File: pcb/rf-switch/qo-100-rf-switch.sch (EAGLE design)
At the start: 40 parts, among them CON1 4P-SH-SIDE, U1 F2915NBGK, U2 ADP7142AUJZ-3.3, U3 MCP23008

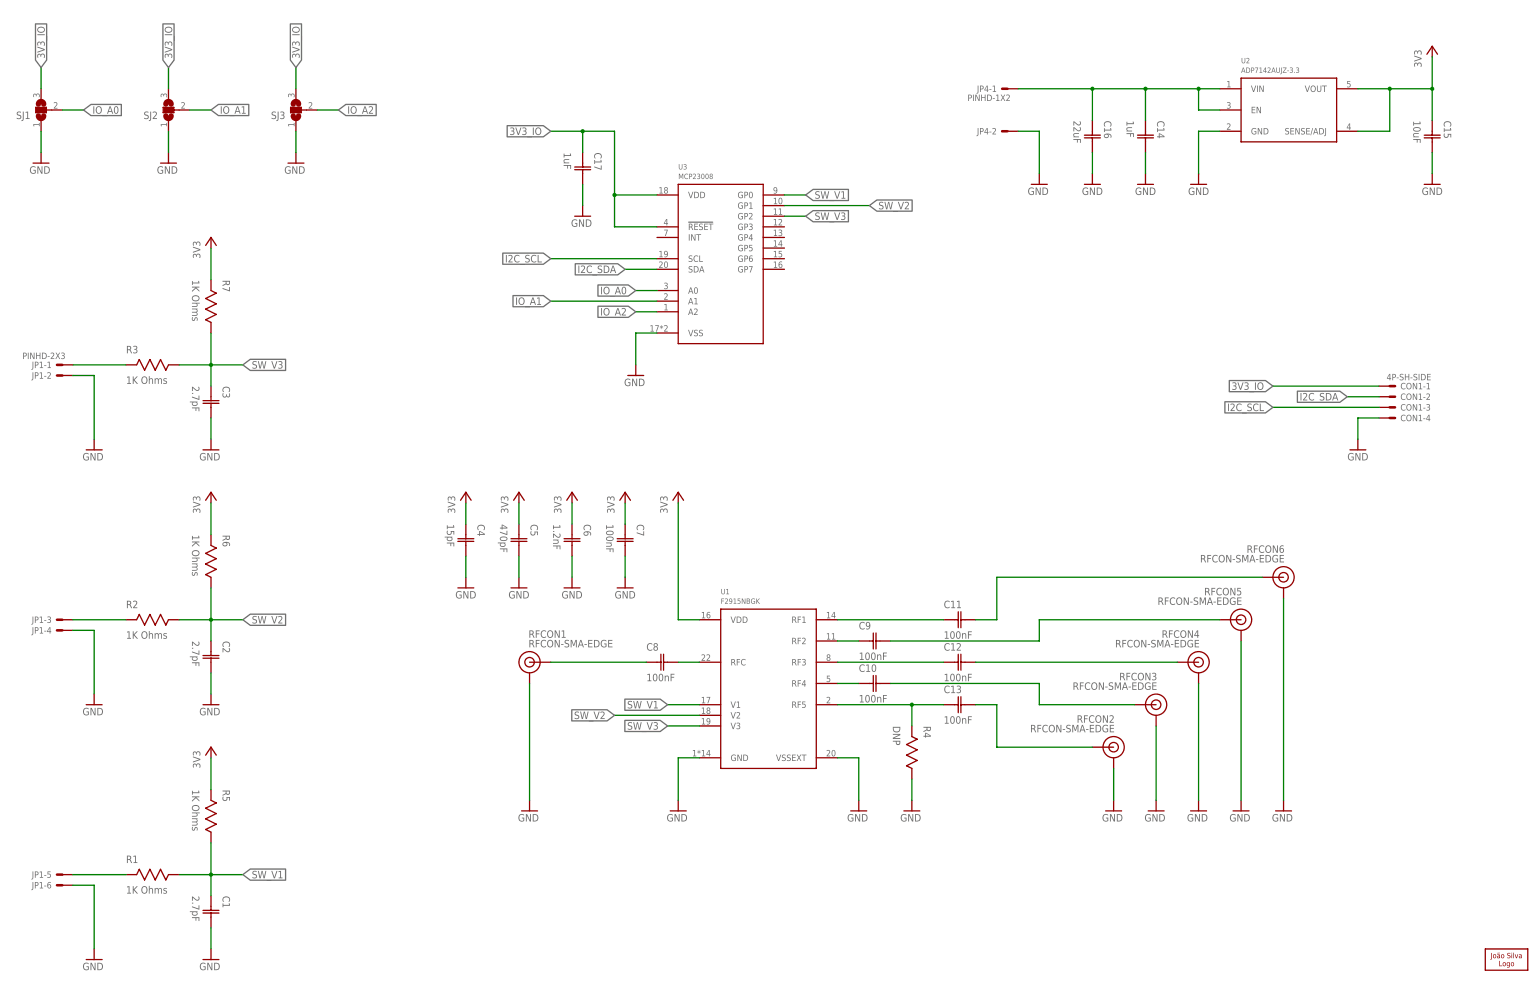
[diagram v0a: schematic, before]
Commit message: RF Switch v2: Allow chosing interface or standalone power in software
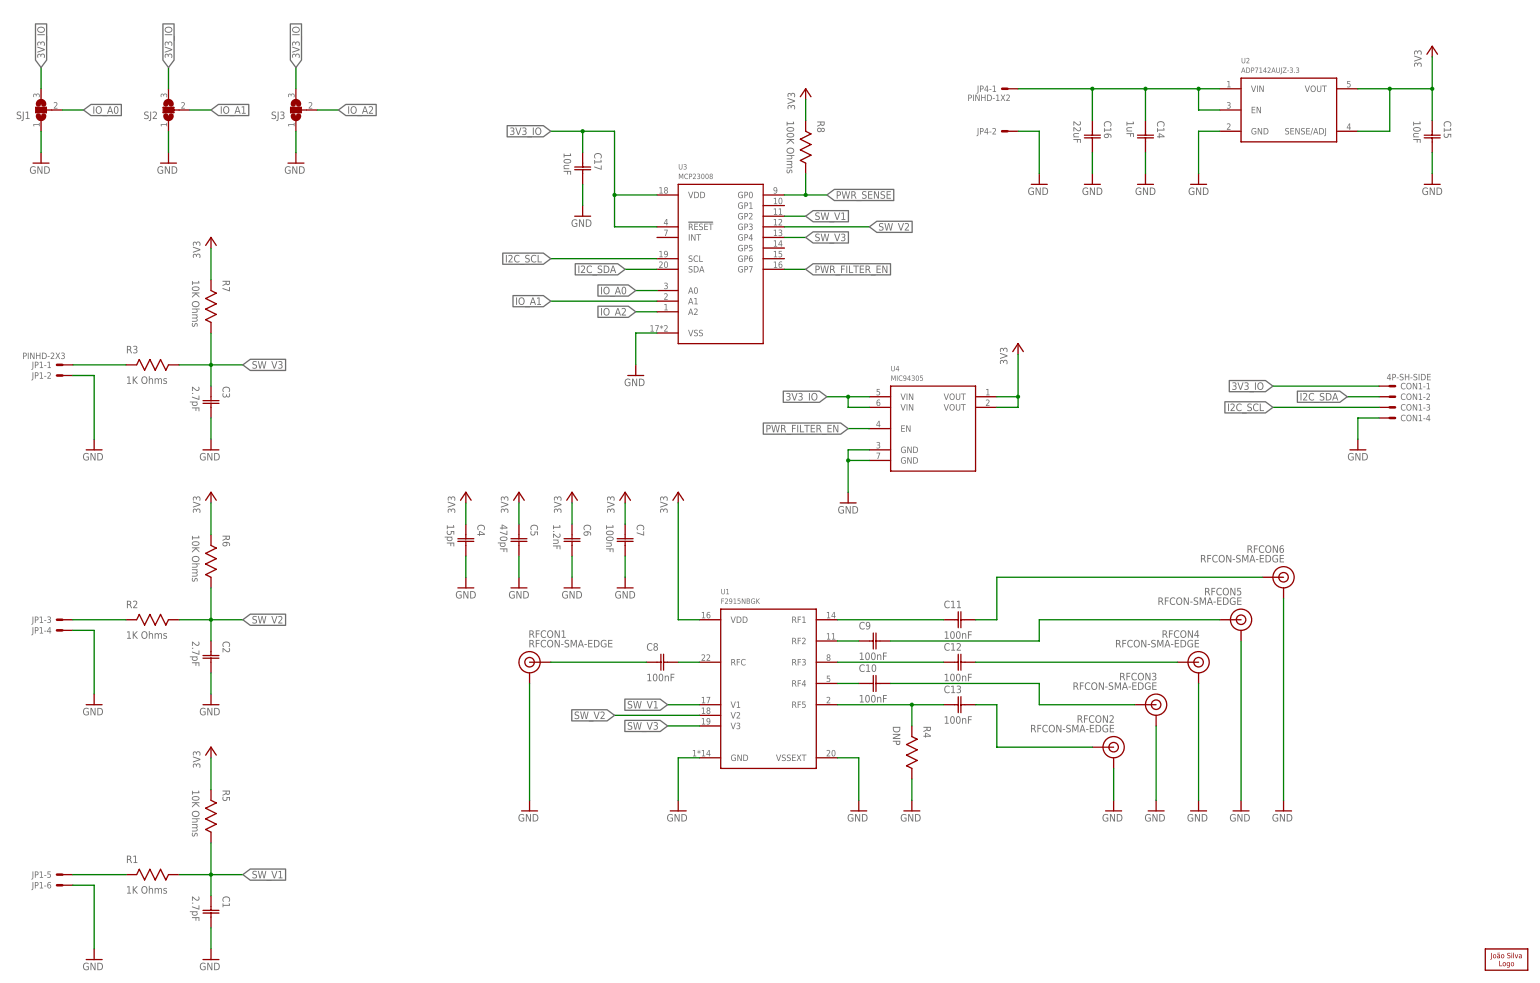
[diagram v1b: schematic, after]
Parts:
- added R8: 100K Ohms, Resistor:RESISTOR-0603
- added U4: MIC94305, Microchip:MIC94305
- C17: value 1uF -> 10uF
- R5, R6, R7: value 1K Ohms -> 10K Ohms
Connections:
- new net PWR_FILTER_EN: U3.GP7, U4.EN
- new net PWR_SENSE: R8.1, U3.GP0
- net 3V3: now also R8.2, U4.VOUT@0, U4.VOUT@1
- net 3V3_IO: now also U4.VIN@0, U4.VIN@1
- net GND: now also U4.GND@0, U4.GND@1
- net SW_V1: now also U3.GP2; no longer U3.GP0
- net SW_V2: now also U3.GP3; no longer U3.GP1
- net SW_V3: now also U3.GP4; no longer U3.GP2
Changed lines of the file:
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@@
 <attributes>
 <attribute name="CNAME" value="None"/>
-<attribute name="CREVISION" value="1"/>
+<attribute name="CREVISION" value="2"/>
 <attribute name="DESIGNER" value="Joao Silva"/>
 </attributes>
@@
 <part name="CON1" library="JST" deviceset="4P" device="-SH-SIDE"/>
 <part name="JP1" library="Pin Header" deviceset="PINHD-2X3" device="" package3d_urn="urn:adsk.eagle:package:22462/2"/>
-<part name="R5" library="Resistor" deviceset="RESISTOR" device="-0603" value="1K Ohms"/>
+<part name="R5" library="Resistor" deviceset="RESISTOR" device="-0603" value="10K Ohms"/>
 <part name="3V2" library="Supply Symbol" deviceset="3V3" device=""/>
-<part name="R6" library="Resistor" deviceset="RESISTOR" device="-0603" value="1K Ohms"/>
+<part name="R6" library="Resistor" deviceset="RESISTOR" device="-0603" value="10K Ohms"/>
 <part name="3V3" library="Supply Symbol" deviceset="3V3" device=""/>
-<part name="R7" library="Resistor" deviceset="RESISTOR" device="-0603" value="1K Ohms"/>
+<part name="R7" library="Resistor" deviceset="RESISTOR" device="-0603" value="10K Ohms"/>
 <part name="GND25" library="Supply Symbol" deviceset="GND" device=""/>
-<part name="C17" library="Capacitor" deviceset="CAPACITOR" device="-0603" value="1uF"/>
+<part name="C17" library="Capacitor" deviceset="CAPACITOR" device="-0603" value="10uF"/>
 <part name="GND26" library="Supply Symbol" deviceset="GND" device=""/>
 <part name="GND27" library="Supply Symbol" deviceset="GND" device=""/>
@@
 <part name="SJ3" library="Solder Jumper" deviceset="SJ2" device="S"/>
 <part name="GND30" library="Supply Symbol" deviceset="GND" device=""/>
+<part name="U4" library="Microchip" deviceset="MIC94305" device=""/>
+<part name="3V7" library="Supply Symbol" deviceset="3V3" device=""/>
+<part name="GND31" library="Supply Symbol" deviceset="GND" device=""/>
+<part name="R8" library="Resistor" deviceset="RESISTOR" device="-0603" value="100K Ohms"/>
+<part name="3V10" library="Supply Symbol" deviceset="3V3" device=""/>
 </parts>
 <sheets>
@@
 <attribute name="VALUE" x="81.026" y="210.82" size="1.778" layer="96"/>
 </instance>
+<instance part="U4" gate="G$1" x="246.38" y="160.02" smashed="yes">
+<attribute name="NAME" x="226.06" y="163.576" size="1.27" layer="95"/>
+<attribute name="VALUE" x="226.06" y="161.29" size="1.27" layer="96"/>
+</instance>
+<instance part="3V7" gate="G$1" x="256.54" y="167.64" smashed="yes">
+<attribute name="VALUE" x="254" y="165.1" size="1.778" layer="96" rot="R90"/>
+</instance>
+<instance part="GND31" gate="G$1" x="215.9" y="134.62" smashed="yes">
+<attribute name="VALUE" x="215.9" y="129.54" size="1.778" layer="96" align="bottom-center"/>
+</instance>
+<instance part="R8" gate="G$1" x="205.74" y="223.52" smashed="yes" rot="R270">
+<attribute name="VALUE" x="202.9714" y="223.52" size="1.778" layer="96" ratio="10" rot="SR270" align="top-left"/>
+<attribute name="NAME" x="208.5086" y="223.52" size="1.778" layer="95" ratio="10" rot="SR270"/>
+<attribute name="TOLERANCE" x="200.4314" y="223.52" size="1.778" layer="97" ratio="10" rot="SR270" align="top-left"/>
+</instance>
+<instance part="3V10" gate="G$1" x="205.74" y="228.6" smashed="yes">
+<attribute name="VALUE" x="203.2" y="226.06" size="1.778" layer="96" rot="R90"/>
+</instance>
 </instances>
 <busses>
@@
 <wire x1="83.82" y1="215.9" x2="83.82" y2="220.98" width="0.1524" layer="91"/>
 <pinref part="SJ3" gate="G$1" pin="1"/>
+</segment>
+<segment>
+<pinref part="GND31" gate="G$1" pin="GND"/>
+<wire x1="215.9" y1="134.62" x2="215.9" y2="142.24" width="0.1524" layer="91"/>
+<wire x1="215.9" y1="142.24" x2="215.9" y2="144.78" width="0.1524" layer="91"/>
+<wire x1="215.9" y1="144.78" x2="220.98" y2="144.78" width="0.1524" layer="91"/>
+<wire x1="220.98" y1="142.24" x2="215.9" y2="142.24" width="0.1524" layer="91"/>
+<junction x="215.9" y="142.24"/>
+<pinref part="U4" gate="G$1" pin="GND@0"/>
+<pinref part="U4" gate="G$1" pin="GND@1"/>
 </segment>
 </net>
@@
 </segment>
 <segment>
-<wire x1="200.66" y1="205.74" x2="205.74" y2="205.74" width="0.1524" layer="91"/>
-<label x="205.74" y="205.74" size="1.778" layer="95" xref="yes"/>
-<pinref part="U3" gate="G$1" pin="GP0"/>
+<wire x1="200.66" y1="200.66" x2="205.74" y2="200.66" width="0.1524" layer="91"/>
+<label x="205.74" y="200.66" size="1.778" layer="95" xref="yes"/>
+<pinref part="U3" gate="G$1" pin="GP2"/>
 </segment>
 </net>
@@
 </segment>
 <segment>
-<wire x1="200.66" y1="203.2" x2="220.98" y2="203.2" width="0.1524" layer="91"/>
-<label x="220.98" y="203.2" size="1.778" layer="95" xref="yes"/>
-<pinref part="U3" gate="G$1" pin="GP1"/>
+<wire x1="200.66" y1="198.12" x2="220.98" y2="198.12" width="0.1524" layer="91"/>
+<label x="220.98" y="198.12" size="1.778" layer="95" xref="yes"/>
+<pinref part="U3" gate="G$1" pin="GP3"/>
 </segment>
 </net>
@@
 </segment>
 <segment>
-<wire x1="200.66" y1="200.66" x2="205.74" y2="200.66" width="0.1524" layer="91"/>
-<label x="205.74" y="200.66" size="1.778" layer="95" xref="yes"/>
-<pinref part="U3" gate="G$1" pin="GP2"/>
+<wire x1="200.66" y1="195.58" x2="205.74" y2="195.58" width="0.1524" layer="91"/>
+<label x="205.74" y="195.58" size="1.778" layer="95" xref="yes"/>
+<pinref part="U3" gate="G$1" pin="GP4"/>
 </segment>
 </net>
@@
 <pinref part="3V3" gate="G$1" pin="3V3"/>
 <wire x1="63.5" y1="185.42" x2="63.5" y2="193.04" width="0.1524" layer="91"/>
+</segment>
+<segment>
+<pinref part="U4" gate="G$1" pin="VOUT@0"/>
+<pinref part="3V7" gate="G$1" pin="3V3"/>
+<wire x1="251.46" y1="157.48" x2="256.54" y2="157.48" width="0.1524" layer="91"/>
+<wire x1="256.54" y1="157.48" x2="256.54" y2="167.64" width="0.1524" layer="91"/>
+<pinref part="U4" gate="G$1" pin="VOUT@1"/>
+<wire x1="251.46" y1="154.94" x2="256.54" y2="154.94" width="0.1524" layer="91"/>
+<wire x1="256.54" y1="154.94" x2="256.54" y2="157.48" width="0.1524" layer="91"/>
+<junction x="256.54" y="157.48"/>
+</segment>
+<segment>
+<pinref part="R8" gate="G$1" pin="2"/>
+<pinref part="3V10" gate="G$1" pin="3V3"/>
+<wire x1="205.74" y1="223.52" x2="205.74" y2="228.6" width="0.1524" layer="91"/>
 </segment>
 </net>
@@
 <pinref part="SJ3" gate="G$1" pin="3"/>
 </segment>
+<segment>
+<wire x1="220.98" y1="157.48" x2="215.9" y2="157.48" width="0.1524" layer="91"/>
+<label x="210.82" y="157.48" size="1.778" layer="95" rot="R180" xref="yes"/>
+<pinref part="U4" gate="G$1" pin="VIN@0"/>
+<pinref part="U4" gate="G$1" pin="VIN@1"/>
+<wire x1="215.9" y1="157.48" x2="210.82" y2="157.48" width="0.1524" layer="91"/>
+<wire x1="220.98" y1="154.94" x2="215.9" y2="154.94" width="0.1524" layer="91"/>
+<wire x1="215.9" y1="154.94" x2="215.9" y2="157.48" width="0.1524" layer="91"/>
+<junction x="215.9" y="157.48"/>
+</segment>
 </net>
 <net name="IO_A0" class="0">
@@
 </segment>
 </net>
+<net name="PWR_FILTER_EN" class="0">
+<segment>
+<pinref part="U4" gate="G$1" pin="EN"/>
+<wire x1="220.98" y1="149.86" x2="215.9" y2="149.86" width="0.1524" layer="91"/>
+<label x="215.9" y="149.86" size="1.778" layer="95" rot="R180" xref="yes"/>
+</segment>
+<segment>
+<wire x1="200.66" y1="187.96" x2="205.74" y2="187.96" width="0.1524" layer="91"/>
+<label x="205.74" y="187.96" size="1.778" layer="95" xref="yes"/>
+<pinref part="U3" gate="G$1" pin="GP7"/>
+</segment>
+</net>
+<net name="PWR_SENSE" class="0">
+<segment>
+<wire x1="200.66" y1="205.74" x2="205.74" y2="205.74" width="0.1524" layer="91"/>
+<label x="210.82" y="205.74" size="1.778" layer="95" xref="yes"/>
+<pinref part="U3" gate="G$1" pin="GP0"/>
+<pinref part="R8" gate="G$1" pin="1"/>
+<wire x1="205.74" y1="205.74" x2="210.82" y2="205.74" width="0.1524" layer="91"/>
+<wire x1="205.74" y1="210.82" x2="205.74" y2="205.74" width="0.1524" layer="91"/>
+<junction x="205.74" y="205.74"/>
+</segment>
+</net>

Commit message: Added notes on PWR_SENSE and PWR_SWITCH_EN on RF Switch schematic
Signed-off-by: João Silva <jgc3silva@gmail.com>
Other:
- note added: "Always check PWR_SENSE before asserting PWR_FILTER_EN. If PWR_SENSE = 1 and PWR_FILTER_EN = 0, external power is applied and PWR_FILTER_EN should NOT be asserted if this is the case. Doing so will short out both supplies!"
- note added: "PWR_SENSE = 0 -> Not powered PWR_SENSE = 1 -> Powered"
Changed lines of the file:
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@@
 <?xml version="1.0" encoding="utf-8"?>
 <!DOCTYPE eagle SYSTEM "eagle.dtd">
-<eagle version="9.6.1">
+<eagle version="9.6.2">
 <drawing>
 <settings>
@@
 <text x="233.68" y="66.04" size="1.778" layer="98">Install R4 for F2914
 Do not install R4 for F2915</text>
+<text x="213.36" y="210.82" size="1.778" layer="98">PWR_SENSE = 0 -&gt; Not powered
+PWR_SENSE = 1 -&gt; Powered</text>
+<text x="274.32" y="187.96" size="1.778" layer="98" align="center">Always check PWR_SENSE before asserting PWR_FILTER_EN.
+If PWR_SENSE = 1 and PWR_FILTER_EN = 0, external power is
+applied and PWR_FILTER_EN should NOT be asserted if this is the
+case. Doing so will short out both supplies!</text>
 </plain>
 <instances>
